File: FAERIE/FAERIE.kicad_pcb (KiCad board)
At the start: 2 copper layers, 43.4 x 93 mm, 41 parts, among them J1 UV Sensor, J10 12V IN, J11 Batt IN, J2 UV Bulb, J3 Sparkmax PWM, J4 Sparkmax, J5 Laser1, J7 CAN, J8 CAM1, J9 CAM2, Q1 SSM3K329R_LF, U1 D24V22Fx, U2 TJA1051T-3

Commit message: FAERIE 2026 V1
FAERIE April 15, 2026
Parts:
- removed the G*** at (180.3, 128.9)
- removed the G*** at (181.6, 121.0)
- removed the G*** at (182.3, 108.6)
- removed J10: 12V IN, Connector_AMASS:AMASS_XT30PW-M_1x02_P2.50mm_Horizontal
- removed J11: Batt IN, Connector_AMASS:AMASS_XT60PW-M_1x02_P7.20mm_Horizontal
- removed J4: Sparkmax, Connector_AMASS:AMASS_XT60PW-F_1x02_P7.20mm_Horizontal
- removed J5: Laser1, Connector_Molex:Molex_Mini-Fit_Jr_5566-02A_2x01_P4.20mm_Vertical
- removed J7: CAN, Connector_AMASS:AMASS_XT30PW-F_1x02_P2.50mm_Horizontal
- removed J8: CAM1, Core_fp:XT30M_MODIFIED
- removed JP1: SolderJumper_3_Open, Jumper:SolderJumper-3_P1.3mm_Open_Pad1.0x1.5mm_NumberLabels
- removed Q1: SSM3K329R_LF, Core_fp:SOTFL95P240X88-3N
- removed R1: 60, Resistor_SMD:R_0603_1608Metric_Pad0.98x0.95mm_HandSolder
- removed R13: R_5V, Resistor_SMD:R_0603_1608Metric_Pad0.98x0.95mm_HandSolder
- removed the REF** at (192.3, 125.8)
- removed the REF** at (156.9, 48.3)
- removed the REF** at (192.3, 48.3)
- removed SHT30: ~, Connector_Molex:Molex_Mini-Fit_Jr_5566-04A_2x02_P4.20mm_Vertical
- removed U2: TJA1051T-3, Package_SO:SOIC-8_3.9x4.9mm_P1.27mm
- added A4: D24V22F5, FAERIE:D24V22Fx, F.Cu at (73.2, 77.4)
- added A6: MP6603_5690, FAERIE:MP6603-5690, F.Cu at (67.8, 101.1)
- added A7: MP6603_5690, FAERIE:MP6603-5690, F.Cu at (67.8, 125.1)
- added A8: MPQ6612A_5285, FAERIE:MPQ6612A_5285, F.Cu at (42.2, 133.9)
- added C12: 100uF, Capacitor_SMD:C_1210_3225Metric_Pad1.33x2.70mm_HandSolder, F.Cu at (78.1, 55.5)
- added C13: 10uF, Capacitor_SMD:C_0603_1608Metric_Pad1.08x0.95mm_HandSolder, F.Cu at (78.0, 59.5)
- added C14: 100uF, Capacitor_SMD:C_1210_3225Metric_Pad1.33x2.70mm_HandSolder, B.Cu at (58.0, 98.6)
- added C15: 100uF, Capacitor_SMD:C_1210_3225Metric_Pad1.33x2.70mm_HandSolder, B.Cu at (58.0, 122.6)
- added C4: 47 nF, Capacitor_SMD:C_0603_1608Metric_Pad1.08x0.95mm_HandSolder, B.Cu at (99.0, 98.8)
- added C5: 10uF, Capacitor_SMD:C_0603_1608Metric_Pad1.08x0.95mm_HandSolder, B.Cu at (88.0, 67.0)
- added C6: 100pF, Capacitor_SMD:C_0603_1608Metric_Pad1.08x0.95mm_HandSolder, B.Cu at (100.6, 52.6)
- added C7: 100pF, Capacitor_SMD:C_0603_1608Metric_Pad1.08x0.95mm_HandSolder, B.Cu at (96.8, 52.6)
- added D4: TVS, FAERIE:SOD-323HEUS2H_TOS, B.Cu at (82.5, 66.8)
- added D5: 15, Diode_SMD:D_SOD-123, B.Cu at (85.0, 63.6)
- added D9: TVS, FAERIE:SOD-323HEUS2H_TOS, F.Cu at (77.5, 63.0)
- added G***: SHC_Logo, FAERIE:SHC_Logo, F.Cu at (85.5, 168.5)
- added G***: ASTRA_Logo, FAERIE:ASTRA_Logo, F.Cu at (97.5, 168.5)
- added J12: Sparkmax 1 Pwr, Connector_AMASS:AMASS_XT60PW-F_1x02_P7.20mm_Horizontal, F.Cu at (48.9, 180.1)
- added J13: Lin Actuator 1 (Large), Connector_AMASS:AMASS_XT30U-F_1x02_P5.0mm_Vertical, F.Cu at (62.9, 162.3)
- added J15: Lasers, Connector_Molex:Molex_Mini-Fit_Jr_5566-04A_2x02_P4.20mm_Vertical, F.Cu at (47.3, 125.0)
- added J16: SHT30, Connector_Molex:Molex_Mini-Fit_Jr_5566-04A_2x02_P4.20mm_Vertical, F.Cu at (106.5, 60.7)
- added J17: Lin Actuator 2 (Small), Connector_AMASS:AMASS_XT30U-F_1x02_P5.0mm_Vertical, F.Cu at (49.2, 162.0)
- added J19: Sparkmax PWM 1, Connector_AMASS:AMASS_XT30U-F_1x02_P5.0mm_Vertical, F.Cu at (49.0, 170.5)
- added J20: Sparkmax PWM 2, Connector_AMASS:AMASS_XT30U-F_1x02_P5.0mm_Vertical, F.Cu at (62.9, 170.5)
- added J21: Sparkmax 2 Pwr, Connector_AMASS:AMASS_XT60PW-F_1x02_P7.20mm_Horizontal, F.Cu at (73.7, 180.1)
- added J22: Fan Pwr, Connector_AMASS:AMASS_XT60PW-F_1x02_P7.20mm_Horizontal, F.Cu at (97.9, 180.1)
- added J23: Stepper Motor 1, Connector_Molex:Molex_Mini-Fit_Jr_5566-04A_2x02_P4.20mm_Vertical, F.Cu at (47.0, 88.9)
- added J24: Stepper Motor 2, Connector_Molex:Molex_Mini-Fit_Jr_5566-04A_2x02_P4.20mm_Vertical, F.Cu at (47.0, 112.9)
- added J25: Stepper 1 Microstep Control, Connector_PinHeader_2.54mm:PinHeader_2x02_P2.54mm_Vertical, F.Cu at (70.8, 97.3)
- added J26: Stepper 2 Microstep Control, Connector_PinHeader_2.54mm:PinHeader_2x02_P2.54mm_Vertical, F.Cu at (70.5, 121.3)
- added J6: Cam 1 Pwr Conn, Connector_AMASS:AMASS_XT30U-F_1x02_P5.0mm_Vertical, F.Cu at (48.0, 66.0)
- added Q2: SSM3K329R_LF, FAERIE:SOT-23F_TOS, B.Cu at (71.3, 129.0)
- added Q3: PMOS, Package_TO_SOT_SMD:TO-252-2, B.Cu at (81.4, 58.6)
- added R17: 50k, Resistor_SMD:R_0603_1608Metric_Pad0.98x0.95mm_HandSolder, B.Cu at (82.5, 52.1)
- added R19: 0Ω, Resistor_SMD:R_0603_1608Metric_Pad0.98x0.95mm_HandSolder, B.Cu at (66.4, 129.0)
- added R20: 10k, Resistor_SMD:R_0603_1608Metric_Pad0.98x0.95mm_HandSolder, B.Cu at (102.0, 146.5)
- added R21: 10k, Resistor_SMD:R_0603_1608Metric_Pad0.98x0.95mm_HandSolder, B.Cu at (101.9, 157.0)
- added REF**: MountingHole_3.2mm_M3, MountingHole:MountingHole_3.2mm_M3, F.Cu at (38.3, 46.1)
- added REF**: MountingHole_3.2mm_M3, MountingHole:MountingHole_3.2mm_M3, F.Cu at (115.3, 46.1)
- added REF**: MountingHole_3.2mm_M3, MountingHole:MountingHole_3.2mm_M3, F.Cu at (38.3, 184.6)
- added REF**: MountingHole_3.2mm_M3, MountingHole:MountingHole_3.2mm_M3, F.Cu at (115.3, 184.1)
- added U4: ESP32 S3 DevKit, FAERIE:ESP32-S3-DevKit_No_Keep-Out_Zone, F.Cu at (107.1, 124.5)
- A1: value Adafruit Feather ESP32 V2 -> VNH5019_1451; footprint Module:Adafruit_Feather -> FAERIE:VNH5019_1451
- C1: value 100nF -> 4.7 nF
- C2: value 4.7nF -> 100uF; footprint Capacitor_SMD:C_0603_1608Metric_Pad1.08x0.95mm_HandSolder -> Capacitor_SMD:C_1210_3225Metric_Pad1.33x2.70mm_HandSolder
- C3: value 1 uF -> 100 nF
- D1: value VBATT -> BATT
- J1: value UV Sensor -> 4s Batt; footprint Connector_Molex:Molex_Mini-Fit_Jr_5566-04A_2x02_P4.20mm_Vertical -> Connector_AMASS:AMASS_XT60PW-M_1x02_P7.20mm_Horizontal
- J2: value UV Bulb -> 12V; footprint Connector_Molex:Molex_Mini-Fit_Jr_5566-02A_2x01_P4.20mm_Vertical -> Connector_AMASS:AMASS_XT30PW-M_1x02_P2.50mm_Horizontal
- J3: value Sparkmax PWM -> VIC CAN; footprint Connector_Molex:Molex_Mini-Fit_Jr_5566-02A_2x01_P4.20mm_Vertical -> Connector_AMASS:AMASS_XT30PW-F_1x02_P2.50mm_Horizontal; moved to B.Cu
- J9: value CAM2 -> CAM 2 Pwr Conn; footprint Core_fp:XT30M_MODIFIED -> Connector_AMASS:AMASS_XT30U-F_1x02_P5.0mm_Vertical
- R10: value R_12V -> R_5V; moved to B.Cu
- R11, R12: value 10 kΩ -> 60
- R2: value 60 -> 10k
- R3: value 330 -> 10k
- R4: value R_US -> R_BATT
- R5: value 10 kΩ -> 10k
- R6: value 3.1 kΩ -> 3.32k
- R7: value R_BATT -> 10k; moved to B.Cu
- R8: value 10 kΩ -> 2.21k
- R9: value 3.8 kΩ -> R_12V
- U1: value D24V22Fx -> TJA1051T/3; footprint Core_fp:D24V22Fx -> Package_SO:SOIC-8_3.9x4.9mm_P1.27mm; moved to B.Cu
- moved D1 138.7 mm to (55.0, 52.5)
- moved R9 136.8 mm to (59.9, 56.1), turned to 0 degrees
- moved R10 133.5 mm to (59.9, 58.6)
- moved D2 133.2 mm to (60.1, 55.1)
- moved J1 122.1 mm to (66.6, 50.8)
- moved R4 121.2 mm to (59.9, 53.6)
- moved R7 120.1 mm to (77.0, 74.1)
- moved R8 116.2 mm to (77.0, 72.6), turned to 180 degrees
- moved J9 114.8 mm to (48.0, 74.0)
- moved R5 114.6 mm to (77.0, 77.1)
- moved R6 114.1 mm to (77.0, 78.6)
- moved R2 107.9 mm to (83.9, 113.1), turned to 180 degrees
- moved D3 102.9 mm to (55.0, 57.7)
- moved C2 98.6 mm to (85.5, 67.5)
- moved A1 97.8 mm to (107.3, 161.8)
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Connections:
- A1 pad 1: unconnected-(A1-~{RESET}-Pad1) -> /LINAC1_FIN
- A1 pad 10: unconnected-(A1-IO_4/A5-Pad10) -> GND
- A1 pad 11: unconnected-(A1-SCK/IO5-Pad11) -> /LINAC1_NEG
- A1 pad 12: unconnected-(A1-MOSI/IO19-Pad12) -> /LINAC1_POS
- A1 pad 13: unconnected-(A1-MISO/IO21-Pad13) -> GND
- A1 pad 14: /RXTransceiver -> +12V
- A1 pad 15: /TXtransceiver -> unconnected-(A1-CS_DIS-Pad15)
- A1 pad 2: +3.3V -> unconnected-(A1-ENA/DIAGA-Pad2)
- A1 pad 3: unconnected-(A1-NC-Pad3) -> +3.3V
- A1 pad 4: GND -> unconnected-(A1-CS-Pad4)
- A1 pad 6: unconnected-(A1-IO25/A1-Pad6) -> /LINAC1_RIN
- A1 pad 7: /5V_ADC -> +3.3V
- A1 pad 8: /12V_ADC -> GND
- A1 pad 9: /BATT_ADC -> unconnected-(A1-VOUT-Pad9)
- C1 pad 1: +3.3V -> GND
- C1 pad 2: GND -> Net-(C1-Pad2)
- C2 pad 1: Net-(JP1-C) -> +12V
- C3 pad 2: GND -> +3.3V
- J1 pad 2: +3.3V -> +BATT
- J2 pad 1: Net-(J2-Pin_1) -> GND
- J2 pad 2: +12V -> /12V_IN
- J3 pad 1: GND -> /CAN_L
- J3 pad 2: /Sparkmax_PWM__A5 -> /CAN_H
- R10 pad 1: +12V -> +5V
- R10 pad 2: Net-(D2-A) -> Net-(D3-A)
- R11 pad 1: +5V -> /CAN_H
- R11 pad 2: /5V_ADC -> Net-(C1-Pad2)
- R12 pad 1: /5V_ADC -> Net-(C1-Pad2)
- R12 pad 2: GND -> /CAN_L
- R2 pad 1: Net-(JP1-A) -> +5V
- R2 pad 2: /CAN_L -> /5V_ADC
- R3 pad 1: GND -> /5V_ADC
- R3 pad 2: Net-(J2-Pin_1) -> GND
- R4 pad 1: Net-(J5-Pin_1) -> +BATT
- R4 pad 2: Net-(Q1-Pad3) -> Net-(D1-A)
- R5 pad 1: +BATT -> +12V
- R5 pad 2: /BATT_ADC -> /12V_ADC
- R6 pad 1: /BATT_ADC -> /12V_ADC
- R7 pad 2: Net-(D1-A) -> /BATT_ADC
- R8 pad 1: +12V -> /BATT_ADC
- R8 pad 2: /12V_ADC -> GND
- R9 pad 1: /12V_ADC -> +12V
- R9 pad 2: GND -> Net-(D2-A)
- U1 pad 1: unconnected-(U1-PG-Pad1) -> /CAN_TX
- U1 pad 2: unconnected-(U1-EN-Pad2) -> GND
- U1 pad 3: +BATT -> +5V
- U1 pad 4: GND -> /CAN_RX
- U1 pad 5: +5V -> +3.3V
- U1 pad 6: GND -> /CAN_L
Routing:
- net +5V: track 136.6 -> 371.8 mm, vias 1 -> 2
- net /SPARK1_PWM: track 0.00 -> 136.2 mm
- net /SPARK2_PWM: track 0.00 -> 115.4 mm
- net +12V: track 107.9 -> 201.8 mm, vias 2 -> 1
- net /LINAC2_RIN: track 0.00 -> 77.1 mm, vias 0 -> 1
- net /LINAC2_FIN: track 0.00 -> 77.1 mm, vias 0 -> 1
- net /I2C_SDA: track 0.00 -> 76.5 mm
- net +3.3V: track 80.2 -> 151.0 mm, vias 1 -> 0
- net +BATT: track 152.5 -> 217.3 mm, vias 0 -> 1
- net /LINAC1_FIN: track 0.00 -> 53.9 mm
- net /I2C_SCL: track 0.00 -> 46.1 mm
- net /LINAC1_RIN: track 0.00 -> 36.4 mm
- net /I2C_SCL_18: track 32.3 -> 0.00 mm
- net /LINAC2_POS: track 0.00 -> 28.3 mm
- net /I2C_SDA_17: track 27.4 -> 0.00 mm
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- added copper zone on B.Cu, net /12V_IN
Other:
- board size 43.4 x 93 mm -> 87 x 148 mm
- rule pad_to_mask_clearance: 0 -> 0.038
- board text added: "*"
- board text added: "0Ω"
- board text added: "1/2"
- board text added: "1/4"
- board text added: "1/8"
- board text added: "100 nF"
- board text added: "100uF"
- board text added: "10k"
- board text added: "10uF"
- board text added: "12V_ADC"
- board text added: "2.21k"
- board text added: "3.32k"
- board text added: "3.3V"
- board text added: "3V3"
- board text added: "47 nF"
- board text added: "4s Batt"
- board text added: "50k"
- board text added: "5V_ADC"
- board text added: "Antenna"
- board text added: "CAN_RX"
- board text added: "CAN_TX"
- board text added: "CS"
- board text added: "CS_DIS"
- board text added: "Cam 1"
- board text added: "Cam 2"
- board text added: "Camera Pwr"
- board text added: "D24V22F5 5V Buck"
- board text added: "DIR"
- board text added: "ESP32 S3 DevKit"
- board text added: "FAERIE ASTRA, SHC at UAH 87 x 148 mm"
- board text added: "Fan Pwr"
- board text added: "I2C Sensor"
- board text added: "I2C_SCL"
- board text added: "I2C_SDA"
- board text added: "IN1"
- board text added: "IN2"
- board text added: "INA"
- board text added: "INB"
- board text added: "In: 4-36V Out: 5V 2.5A"
- board text added: "LASER_NMOS"
- board text added: "LINAC1_FIN"
- board text added: "LINAC1_RIN"
- board text added: "Laser"
- board text added: "Lasers"
- board text added: "Lin Ac Lg"
- board text added: "Lin Ac Sm"
- board text added: "M1"
- board text added: "M2"
- board text added: "Motor Controller"
- board text added: "NEG"
- board text added: "NMOS"
- board text added: "OUT1"
- board text added: "OUT2"
- board text added: "OUTA"
- board text added: "OUTB"
- board text added: "OUTC"
- board text added: "OUTD"
- board text added: "PJD60P04E-AU"
- board text added: "POS"
- board text added: "PWM"
- board text added: "Pololu"
- board text added: "Polulu MP6603"
- board text added: "Polulu MP6603 Motor Controller"
- board text added: "Polulu MPQ6612A Motor Controller"
- board text added: "Polulu VNH5019 Motor Controller"
- board text added: "SHC FAERIE 4/15/26"
- board text added: "SPARK_PWM"
- board text added: "STEP"
- board text added: "Spark PWM 1"
- board text added: "Spark PWM 2"
- board text added: "Sparkmax 1 Pwr"
- board text added: "Sparkmax 2 Pwr"
- board text added: "Stepper 1"
- board text added: "Stepper 2"
- board text added: "Stepper Motor 1"
- board text added: "Stepper Motor 2"
- board text added: "TVS"
- board text added: "VBATT_ADC"
- board text added: "VDD"
- board text added: "Vic CAN"
- board text added: "XT30-M"
- board text added: "XT60-F"
- board text added: "XT60-M"
- board text added: "Zener"
- board text added: "{ "ViaStitching": "0.2", "GND": { "HSpacing": "1", "VSpacing": "1", "HOffset": "0", "VOffset": "0", "Clearance": "1", "Randomize": false } }"
- board text added: "{ "ViaStitching": "0.2", "GND": { "HSpacing": "1.27", "VSpacing": "1.27", "HOffset": "0", "VOffset": "0", "Clearance": "0.2", "Randomize": false } }"
- board text added: "{ "ViaStitching": "0.2", "GND": { "HSpacing": "2", "VSpacing": "2", "HOffset": "0", "VOffset": "0", "Clearance": "0.5", "Randomize": false } }"
- board text added: "{ "ViaStitching": "0.2", "GND": { "HSpacing": "2", "VSpacing": "2", "HOffset": "0", "VOffset": "0", "Clearance": "1", "Randomize": false } }"
- board text added: "{ "ViaStitching": "0.2", "GND": { "HSpacing": "2.2", "VSpacing": "2.2", "HOffset": "0", "VOffset": "0", "Clearance": "1", "Randomize": false } }"
- board text added: "{ "ViaStitching": "0.2", "GND": { "HSpacing": "2.5", "VSpacing": "2.5", "HOffset": "0", "VOffset": "0", "Clearance": ".25", "Randomize": false } }"
- board text added: "{ "ViaStitching": "0.2", "GND": { "HSpacing": "2.5", "VSpacing": "2.5", "HOffset": "0", "VOffset": "0", "Clearance": ".5", "Randomize": false } }"
- board text added: "{ "ViaStitching": "0.2", "GND": { "HSpacing": "2.5", "VSpacing": "2.5", "HOffset": "0", "VOffset": "0", "Clearance": "0.5", "Randomize": false } }"
- board text added: "{ "ViaStitching": "0.2", "GND": { "HSpacing": "2.5", "VSpacing": "2.5", "HOffset": "0", "VOffset": "0", "Clearance": "1", "Randomize": false } }"
- board text added: "{ "ViaStitching": "0.2", "GND": { "HSpacing": "3", "VSpacing": "3", "HOffset": "0", "VOffset": "0", "Clearance": ".5", "Randomize": false } }"
- board text added: "{ "ViaStitching": "0.2", "GND": { "HSpacing": "3", "VSpacing": "3", "HOffset": "0", "VOffset": "0", "Clearance": "0", "Randomize": false } }"
- board text added: "{ "ViaStitching": "0.2", "GND": { "HSpacing": "3", "VSpacing": "3", "HOffset": "0", "VOffset": "0", "Clearance": "1", "Randomize": false } }"
- board text added: "{ "ViaStitching": "0.2", "GND": { "HSpacing": "4", "VSpacing": "4", "HOffset": "0", "VOffset": "0", "Clearance": "1", "Randomize": false } }"
- board text added: "{ "ViaStitching": "0.2", "GND": { "HSpacing": "4", "VSpacing": "4", "HOffset": "0", "VOffset": "0", "Clearance": "4", "Randomize": false } }"
- board text added: "~SLEEP"
- board text removed: "#4-40"
- board text removed: "+ CAM 12V -"
- board text removed: "+ Laser -"
- board text removed: "+ Spark PWM -"
- board text removed: "+ UV Bulb -"
- board text removed: "+14.8V"
- board text removed: "+3.3V"
- board text removed: "0.1 μF"
- board text removed: "1.0 μF"
- board text removed: "10 kΩ"
- board text removed: "3.1 kΩ"
- board text removed: "3.8 kΩ"
- board text removed: "30"
- board text removed: "4S BATT"
- board text removed: "5VOUT"
- board text removed: "60"
- board text removed: "60Ω"
- board text removed: "Adafruit ESP32 Feather V2"
- board text removed: "CAN Transceiver"
- board text removed: "D"
- board text removed: "EN"
- board text removed: "F"
- board text removed: "FAERIE V1 01/26/25"
- board text removed: "Fouth Mounting 4-40 screw was deleted because of placemnet issues"
- board text removed: "G"
- board text removed: "IN: 5.3-36V OUT: 5V 2.5A"
- board text removed: "J12"
- board text removed: "JLCJLCJLCJLC"
- board text removed: "M"
- board text removed: "PG"
- board text removed: "S"
- board text removed: "SSM3K329R_LF"
- board text removed: "UV Sensor"
- board text removed: "VIC CAN"

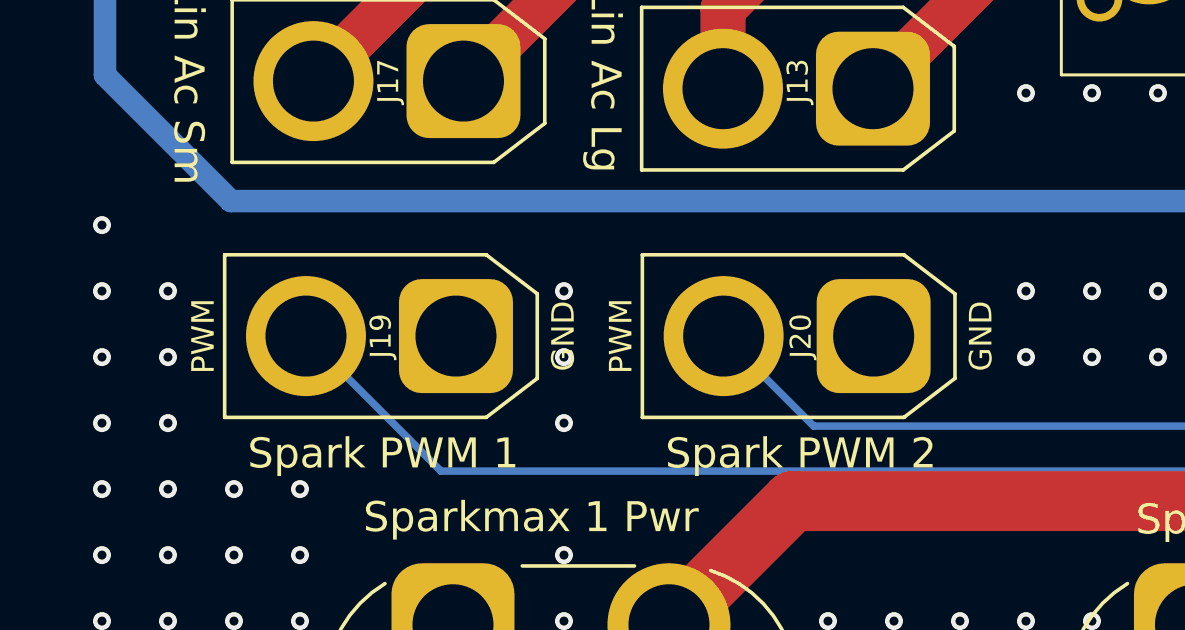
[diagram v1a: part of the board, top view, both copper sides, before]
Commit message: FAERIE 2026 r1.01
Changed Sparkmax PWM 1 and 2 from XT-30 connectors to Molex
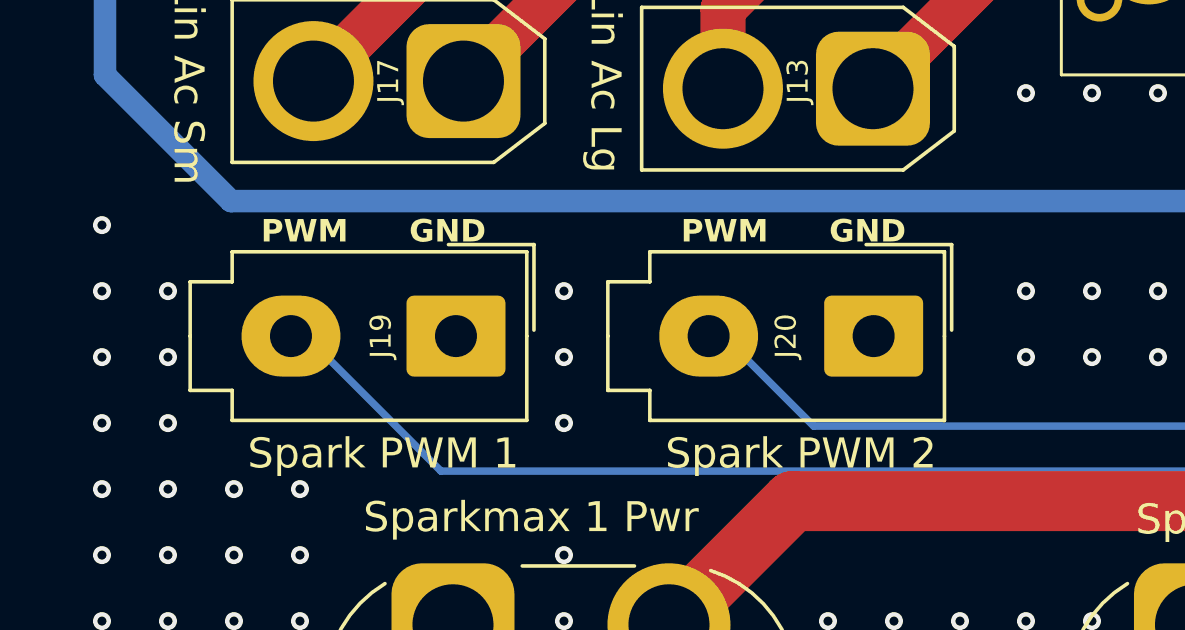
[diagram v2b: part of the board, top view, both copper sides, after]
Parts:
- J19, J20: footprint Connector_AMASS:AMASS_XT30U-F_1x02_P5.0mm_Vertical -> Connector_Molex:Molex_Mini-Fit_Jr_5566-02A_2x01_P4.20mm_Vertical
- turned J19 to -90 degrees
- turned J20 to -90 degrees
